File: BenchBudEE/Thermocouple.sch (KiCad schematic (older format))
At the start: 14 parts

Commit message: Placed the relay components.
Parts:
- gave numbers to parts that had none: 11
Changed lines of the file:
@@
 Sheet 2 9
 Title ""
-Date "19 feb 2014"
+Date "20 feb 2014"
 Rev ""
 Comp ""
@@
 CS_N
 $Comp
-L LM324 U?
-U 1 1 52F20391
+L LM324 U4
+U 3 1 52F20391
 P 9000 1850
-F 0 "U?" H 9050 2050 60  0000 C CNN
+F 0 "U4" H 9050 2050 60  0000 C CNN
 F 1 "LM324" H 9150 1650 50  0000 C CNN
 F 2 "" H 9000 1850 60  0000 C CNN
 F 3 "" H 9000 1850 60  0000 C CNN
-	1    9000 1850
+	3    9000 1850
 	-1   0    0    -1
 $EndComp
 $Comp
-L LM324 U?
-U 1 1 52F2039E
+L LM324 U4
+U 4 1 52F2039E
 P 9050 4350
-F 0 "U?" H 9100 4550 60  0000 C CNN
+F 0 "U4" H 9100 4550 60  0000 C CNN
 F 1 "LM324" H 9200 4150 50  0000 C CNN
 F 2 "" H 9050 4350 60  0000 C CNN
 F 3 "" H 9050 4350 60  0000 C CNN
-	1    9050 4350
+	4    9050 4350
 	-1   0    0    1
 $EndComp
 $Comp
-L LM324 U?
+L LM324 U4
 U 1 1 52F203A9
 P 6250 3100
-F 0 "U?" H 6300 3300 60  0000 C CNN
+F 0 "U4" H 6300 3300 60  0000 C CNN
 F 1 "LM324" H 6400 2900 50  0000 C CNN
 F 2 "" H 6250 3100 60  0000 C CNN
@@
 $EndComp
 $Comp
-L LM324 U?
-U 1 1 52F203B8
+L LM324 U4
+U 2 1 52F203B8
 P 7650 5800
-F 0 "U?" H 7700 6000 60  0000 C CNN
+F 0 "U4" H 7700 6000 60  0000 C CNN
 F 1 "LM324" H 7800 5600 50  0000 C CNN
 F 2 "" H 7650 5800 60  0000 C CNN
 F 3 "" H 7650 5800 60  0000 C CNN
-	1    7650 5800
+	2    7650 5800
 	-1   0    0    -1
 $EndComp
 $Comp
-L R R?
+L R R11
 U 1 1 52F204D2
 P 8200 2250
-F 0 "R?" V 8280 2250 40  0000 C CNN
+F 0 "R11" V 8280 2250 40  0000 C CNN
 F 1 "R" V 8207 2251 40  0000 C CNN
 F 2 "~" V 8130 2250 30  0000 C CNN
@@
 $EndComp
 $Comp
-L R R?
+L R R12
 U 1 1 52F204DF
 P 8200 3100
-F 0 "R?" V 8280 3100 40  0000 C CNN
+F 0 "R12" V 8280 3100 40  0000 C CNN
 F 1 "R" V 8207 3101 40  0000 C CNN
 F 2 "~" V 8130 3100 30  0000 C CNN
@@
 $EndComp
 $Comp
-L R R?
+L R R13
 U 1 1 52F204E6
 P 8200 3900
-F 0 "R?" V 8280 3900 40  0000 C CNN
+F 0 "R13" V 8280 3900 40  0000 C CNN
 F 1 "R" V 8207 3901 40  0000 C CNN
 F 2 "~" V 8130 3900 30  0000 C CNN
@@
 $EndComp
 $Comp
-L R R?
+L R R9
 U 1 1 52F2053E
 P 7300 1850
-F 0 "R?" V 7380 1850 40  0000 C CNN
+F 0 "R9" V 7380 1850 40  0000 C CNN
 F 1 "R" V 7307 1851 40  0000 C CNN
 F 2 "~" V 7230 1850 30  0000 C CNN
@@
 $EndComp
 $Comp
-L R R?
+L R R7
 U 1 1 52F2054F
 P 5550 1850
-F 0 "R?" V 5630 1850 40  0000 C CNN
+F 0 "R7" V 5630 1850 40  0000 C CNN
 F 1 "R" V 5557 1851 40  0000 C CNN
 F 2 "~" V 5480 1850 30  0000 C CNN
@@
 $EndComp
 $Comp
-L R R?
+L R R10
 U 1 1 52F20559
 P 7350 4350
-F 0 "R?" V 7430 4350 40  0000 C CNN
+F 0 "R10" V 7430 4350 40  0000 C CNN
 F 1 "R" V 7357 4351 40  0000 C CNN
 F 2 "~" V 7280 4350 30  0000 C CNN
@@
 $EndComp
 $Comp
-L R R?
+L R R8
 U 1 1 52F20561
 P 5550 4350
-F 0 "R?" V 5630 4350 40  0000 C CNN
+F 0 "R8" V 5630 4350 40  0000 C CNN
 F 1 "R" V 5557 4351 40  0000 C CNN
 F 2 "~" V 5480 4350 30  0000 C CNN
@@
 $EndComp
 $Comp
-L -12V #PWR?
+L -12V #PWR3
 U 1 1 52F21D94
 P 6350 2600
-F 0 "#PWR?" H 6350 2730 20  0001 C CNN
+F 0 "#PWR3" H 6350 2730 20  0001 C CNN
 F 1 "-12V" H 6350 2700 30  0000 C CNN
 F 2 "" H 6350 2600 60  0000 C CNN
@@
 $EndComp
 $Comp
-L -12V #PWR?
+L -12V #PWR6
 U 1 1 52F21DA1
 P 9100 2350
-F 0 "#PWR?" H 9100 2480 20  0001 C CNN
+F 0 "#PWR6" H 9100 2480 20  0001 C CNN
 F 1 "-12V" H 9100 2450 30  0000 C CNN
 F 2 "" H 9100 2350 60  0000 C CNN
@@
 $EndComp
 $Comp
-L -12V #PWR?
+L -12V #PWR7
 U 1 1 52F21DA8
 P 9150 3850
-F 0 "#PWR?" H 9150 3980 20  0001 C CNN
+F 0 "#PWR7" H 9150 3980 20  0001 C CNN
 F 1 "-12V" H 9150 3950 30  0000 C CNN
 F 2 "" H 9150 3850 60  0000 C CNN
@@
 $EndComp
 $Comp
-L +12V #PWR?
+L +12V #PWR4
 U 1 1 52F21DD5
 P 6350 3600
-F 0 "#PWR?" H 6350 3550 20  0001 C CNN
+F 0 "#PWR4" H 6350 3550 20  0001 C CNN
 F 1 "+12V" H 6350 3700 30  0000 C CNN
 F 2 "" H 6350 3600 60  0000 C CNN
@@
 $EndComp
 $Comp
-L +12V #PWR?
+L +12V #PWR5
 U 1 1 52F21DE2
 P 9100 1350
-F 0 "#PWR?" H 9100 1300 20  0001 C CNN
+F 0 "#PWR5" H 9100 1300 20  0001 C CNN
 F 1 "+12V" H 9100 1450 30  0000 C CNN
 F 2 "" H 9100 1350 60  0000 C CNN
@@
 $EndComp
 $Comp
-L +12V #PWR?
+L +12V #PWR8
 U 1 1 52F21DE8
 P 9150 4850
-F 0 "#PWR?" H 9150 4800 20  0001 C CNN
+F 0 "#PWR8" H 9150 4800 20  0001 C CNN
 F 1 "+12V" H 9150 4950 30  0000 C CNN
 F 2 "" H 9150 4850 60  0000 C CNN
@@
 	9150 3950 9150 3850
 $Comp
-L AGND #PWR?
+L AGND #PWR2
 U 1 1 52F21ED2
 P 5150 4550
-F 0 "#PWR?" H 5150 4550 40  0001 C CNN
+F 0 "#PWR2" H 5150 4550 40  0001 C CNN
 F 1 "AGND" H 5150 4480 50  0000 C CNN
 F 2 "" H 5150 4550 60  0000 C CNN
@@
 	5150 4350 5300 4350
 $Comp
-L MCP3550-60-E/SN U?
+L MCP3550-60-E/SN U2
 U 1 1 52F21F8C
 P 2750 3250
-F 0 "U?" H 2200 3600 40  0000 C CNN
+F 0 "U2" H 2200 3600 40  0000 C CNN
 F 1 "MCP3550-60-E/SN" H 2450 3550 40  0000 C CNN
 F 2 "SO8" H 2550 3250 30  0000 C CIN
@@
 	1100 3350 2250 3350
 $Comp
-L MCP3550-60-E/SN U?
+L MCP3550-60-E/SN U3
 U 1 1 52F220D9
 P 2850 5850
-F 0 "U?" H 2300 6200 40  0000 C CNN
+F 0 "U3" H 2300 6200 40  0000 C CNN
 F 1 "MCP3550-60-E/SN" H 2550 6150 40  0000 C CNN
 F 2 "SO8" H 2650 5850 30  0000 C CIN
@@
 $EndComp
 $Comp
-L ZENER D?
+L ZENER D3
 U 1 1 52F22109
 P 9250 6200
-F 0 "D?" H 9250 6300 50  0000 C CNN
+F 0 "D3" H 9250 6300 50  0000 C CNN
 F 1 "ZENER" H 9250 6100 40  0000 C CNN
 F 2 "~" H 9250 6200 60  0000 C CNN
@@
 $EndComp
 $Comp
-L +12V #PWR?
+L +12V #PWR9
 U 1 1 52F22125
 P 9250 5650
-F 0 "#PWR?" H 9250 5600 20  0001 C CNN
+F 0 "#PWR9" H 9250 5600 20  0001 C CNN
 F 1 "+12V" H 9250 5750 30  0000 C CNN
 F 2 "" H 9250 5650 60  0000 C CNN
@@
 $EndComp
 $Comp
-L AGND #PWR?
+L AGND #PWR10
 U 1 1 52F2212B
 P 9250 6750
-F 0 "#PWR?" H 9250 6750 40  0001 C CNN
+F 0 "#PWR10" H 9250 6750 40  0001 C CNN
 F 1 "AGND" H 9250 6680 50  0000 C CNN
 F 2 "" H 9250 6750 60  0000 C CNN
@@
 Connection ~ 6800 5800
 $Comp
-L AGND #PWR?
+L AGND #PWR1
 U 1 1 52F22221
 P 3750 6550
-F 0 "#PWR?" H 3750 6550 40  0001 C CNN
+F 0 "#PWR1" H 3750 6550 40  0001 C CNN
 F 1 "AGND" H 3750 6480 50  0000 C CNN
 F 2 "" H 3750 6550 60  0000 C CNN

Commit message: Associated the Thermocouple components.
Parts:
- removed D3: ZENER, ~, symbol ZENER
- removed U2, U3: MCP3550-60-E/SN, SO8, symbol MCP3550-60-E/SN
- removed unit 2 of U4
- added C10, C11, C6, C7, C8, C9: C, ~, symbol C
- added P2: CONN_3X2, symbol CONN_3X2
- added P3: CONN_2, symbol CONN_2
- added R44, R45: R, ~, symbol R
- added U2: MCP3901, symbol MCP3901
- added U3: LMT84, symbol LMT84
- U4: value LM324 -> OPA4170
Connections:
- net labels added: +5V, REF+, REF-, ~CS, ~DR, ~RESET
- net labels removed: CS_N
- wire segments 47 -> 93
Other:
- note added: "16-24 Bit ADC"
- note added: "2-pin header for\nfuture use if\nneeded."
- note added: "Caps for decoupling (smooth out voltage input) and filtering out any high freq."
- note added: "Jumper to select on\nof those resistors for\nselectable gain."
- note added: "TEMP SENSOR"
- note removed: "16-24Bit ADC"
- note removed: "General Temperature Sensor"

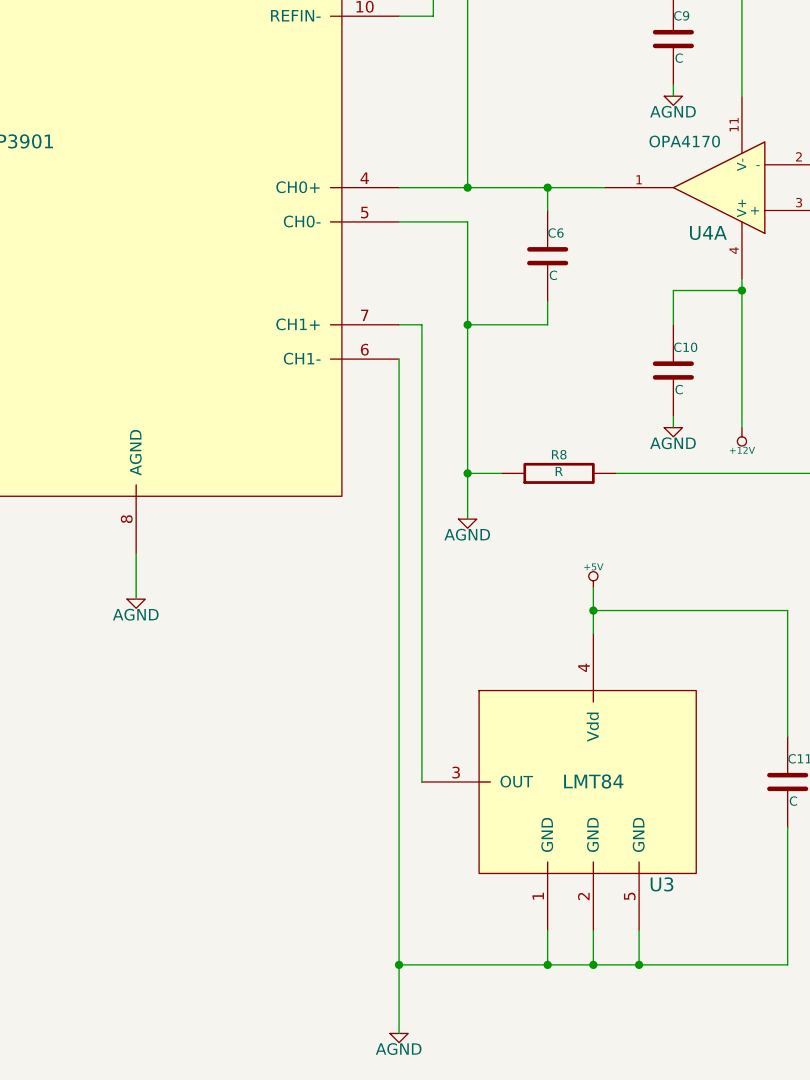
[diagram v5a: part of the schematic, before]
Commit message: Roughly placed the Thermocouple components.
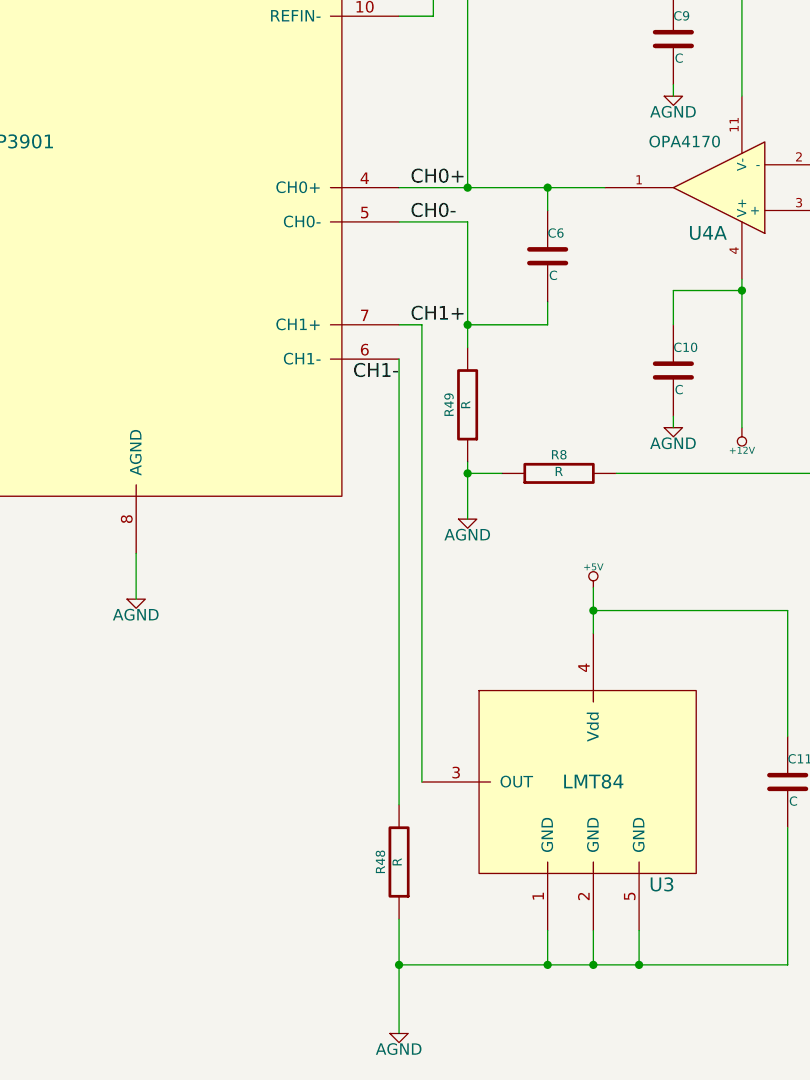
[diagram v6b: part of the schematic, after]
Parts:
- added R48, R49: R, ~, symbol R
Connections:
- net +5V: now also R48.1, R49.1; no longer C6.2, U2.5 (CH0-), U2.6 (CH1-)
- net CH0+: now reaches C6.1, R7.1, U2.4 (CH0+), U4.1
- net CH1+: now reaches U2.7 (CH1+), U3.3 (OUT)
- new net CH0-: C6.2, R49.2, U2.5 (CH0-)
- new net CH1-: R48.2, U2.6 (CH1-)
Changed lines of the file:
@@
 $EndComp
-Wire Wire Line
-	5150 3250 5150 4550
 Wire Wire Line
 	5150 4350 5300 4350
@@
 	4950 3700 4850 3700
 Wire Wire Line
-	4850 3850 4850 6800
-Wire Wire Line
 	4850 6500 6550 6500
 Wire Wire Line
@@
 Text Notes 1400 4150 2    60   ~ 0
 2-pin header for\nfuture use if\nneeded.
+Text Label 4900 3100 0    60   ~ 0
+CH0+
+Text Label 4900 3250 0    60   ~ 0
+CH0-
+Text Label 4900 3700 0    60   ~ 0
+CH1+
+Text Label 4850 3950 2    60   ~ 0
+CH1-
+$Comp
+L R R49
+U 1 1 5307180E
+P 5150 4050
+F 0 "R49" V 5230 4050 40  0000 C CNN
+F 1 "R" V 5157 4051 40  0000 C CNN
+F 2 "~" V 5080 4050 30  0000 C CNN
+F 3 "~" H 5150 4050 30  0000 C CNN
+	1    5150 4050
+	-1   0    0    1
+$EndComp
+Wire Wire Line
+	5150 3250 5150 3800
+Wire Wire Line
+	5150 4300 5150 4550
+$Comp
+L R R48
+U 1 1 530719FC
+P 4850 6050
+F 0 "R48" V 4930 6050 40  0000 C CNN
+F 1 "R" V 4857 6051 40  0000 C CNN
+F 2 "~" V 4780 6050 30  0000 C CNN
+F 3 "~" H 4850 6050 30  0000 C CNN
+	1    4850 6050
+	-1   0    0    1
+$EndComp
+Wire Wire Line
+	4850 6300 4850 6800
+Wire Wire Line
+	4850 3850 4850 5800
 $EndSCHEMATC
